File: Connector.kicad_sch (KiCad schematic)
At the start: 2 parts, among them J1 Conn_01x19, J2 Conn_01x19

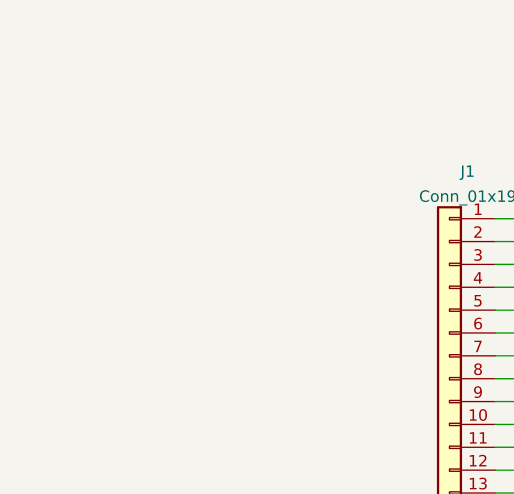
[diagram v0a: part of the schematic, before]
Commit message: Routed most PCB traces
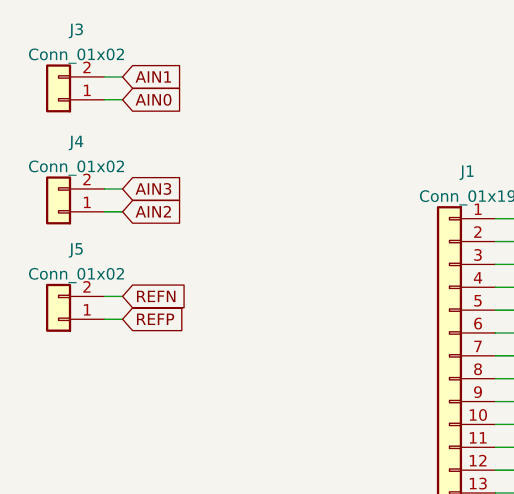
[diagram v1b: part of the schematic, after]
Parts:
- added J3, J4, J5: Conn_01x02, Connector_Molex:Molex_CLIK-Mate_502382-0270_1x02-1MP_P1.25mm_Vertical, symbol Connector_Generic:Conn_01x02
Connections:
- new net AIN0: J3.1 (Pin_1)
- new net AIN1: J3.2 (Pin_2)
- new net AIN2: J4.1 (Pin_1)
- new net AIN3: J4.2 (Pin_2)
- new net REFN: J5.2 (Pin_2)
- new net REFP: J5.1 (Pin_1)
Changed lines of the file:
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@@
   (junction (at 138.684 88.392) (diameter 1.016) (color 0 0 0 0))
   (junction (at 145.034 73.152) (diameter 1.016) (color 0 0 0 0))
+  (wire (pts (xy 48.514 57.404) (xy 50.546 57.404))
+    (stroke (width 0) (type solid) (color 0 0 0 0))
+  )
+  (wire (pts (xy 48.514 59.944) (xy 50.546 59.944))
+    (stroke (width 0) (type solid) (color 0 0 0 0))
+  )
+  (wire (pts (xy 48.514 69.85) (xy 50.546 69.85))
+    (stroke (width 0) (type solid) (color 0 0 0 0))
+  )
+  (wire (pts (xy 48.514 72.39) (xy 50.546 72.39))
+    (stroke (width 0) (type solid) (color 0 0 0 0))
+  )
+  (wire (pts (xy 48.514 81.788) (xy 50.546 81.788))
+    (stroke (width 0) (type solid) (color 0 0 0 0))
+  )
+  (wire (pts (xy 48.514 84.328) (xy 50.546 84.328))
+    (stroke (width 0) (type solid) (color 0 0 0 0))
+  )
   (wire (pts (xy 91.948 73.152) (xy 99.06 73.152))
     (stroke (width 0) (type solid) (color 0 0 0 0))
@@
   (wire (pts (xy 149.098 71.12) (xy 149.098 73.152))
     (stroke (width 0) (type solid) (color 0 0 0 0))
+  )
+  (global_label "AIN1" (shape input) (at 50.546 57.404 0) (fields_autoplaced)
+    (effects (font (size 1.27 1.27)) (justify left))
+    (property "Intersheet References" "${INTERSHEET_REFS}" (id 0) (at 57.0971 57.3246 0)
+      (effects (font (size 1.27 1.27)) (justify left) hide)
+    )
+  )
+  (global_label "AIN0" (shape input) (at 50.546 59.944 0) (fields_autoplaced)
+    (effects (font (size 1.27 1.27)) (justify left))
+    (property "Intersheet References" "${INTERSHEET_REFS}" (id 0) (at 57.0971 59.8646 0)
+      (effects (font (size 1.27 1.27)) (justify left) hide)
+    )
+  )
+  (global_label "AIN3" (shape input) (at 50.546 69.85 0) (fields_autoplaced)
+    (effects (font (size 1.27 1.27)) (justify left))
+    (property "Intersheet References" "${INTERSHEET_REFS}" (id 0) (at 57.0971 69.7706 0)
+      (effects (font (size 1.27 1.27)) (justify left) hide)
+    )
+  )
+  (global_label "AIN2" (shape input) (at 50.546 72.39 0) (fields_autoplaced)
+    (effects (font (size 1.27 1.27)) (justify left))
+    (property "Intersheet References" "${INTERSHEET_REFS}" (id 0) (at 57.0971 72.3106 0)
+      (effects (font (size 1.27 1.27)) (justify left) hide)
+    )
+  )
+  (global_label "REFN" (shape input) (at 50.546 81.788 0) (fields_autoplaced)
+    (effects (font (size 1.27 1.27)) (justify left))
+    (property "Intersheet References" "${INTERSHEET_REFS}" (id 0) (at 57.7019 81.7086 0)
+      (effects (font (size 1.27 1.27)) (justify left) hide)
+    )
+  )
+  (global_label "REFP" (shape input) (at 50.546 84.328 0) (fields_autoplaced)
+    (effects (font (size 1.27 1.27)) (justify left))
+    (property "Intersheet References" "${INTERSHEET_REFS}" (id 0) (at 57.6414 84.2486 0)
+      (effects (font (size 1.27 1.27)) (justify left) hide)
+    )
   )
   (global_label "SENSOR_VP" (shape input) (at 100.076 78.232 0) (fields_autoplaced)
@@
     (pin "1")
   )
+  (symbol (lib_id "Connector_Generic:Conn_01x02") (at 43.434 59.944 180) (unit 1)
+    (in_bom yes) (on_board yes) (fields_autoplaced)
+    (property "Reference" "J3" (id 0) (at 45.466 52.1674 0))
+    (property "Value" "Conn_01x02" (id 1) (at 45.466 54.9425 0))
+    (property "Footprint" "Connector_Molex:Molex_CLIK-Mate_502382-0270_1x02-1MP_P1.25mm_Vertical" (id 2) (at 43.434 59.944 0)
+      (effects (font (size 1.27 1.27)) hide)
+    )
+    (property "Datasheet" "~" (id 3) (at 43.434 59.944 0)
+      (effects (font (size 1.27 1.27)) hide)
+    )
+    (pin "1")
+    (pin "2")
+  )
+  (symbol (lib_id "Connector_Generic:Conn_01x02") (at 43.434 72.39 180) (unit 1)
+    (in_bom yes) (on_board yes) (fields_autoplaced)
+    (property "Reference" "J4" (id 0) (at 45.466 64.6134 0))
+    (property "Value" "Conn_01x02" (id 1) (at 45.466 67.3885 0))
+    (property "Footprint" "Connector_Molex:Molex_CLIK-Mate_502382-0270_1x02-1MP_P1.25mm_Vertical" (id 2) (at 43.434 72.39 0)
+      (effects (font (size 1.27 1.27)) hide)
+    )
+    (property "Datasheet" "~" (id 3) (at 43.434 72.39 0)
+      (effects (font (size 1.27 1.27)) hide)
+    )
+    (pin "1")
+    (pin "2")
+  )
+  (symbol (lib_id "Connector_Generic:Conn_01x02") (at 43.434 84.328 180) (unit 1)
+    (in_bom yes) (on_board yes) (fields_autoplaced)
+    (property "Reference" "J5" (id 0) (at 45.466 76.5514 0))
+    (property "Value" "Conn_01x02" (id 1) (at 45.466 79.3265 0))
+    (property "Footprint" "Connector_Molex:Molex_CLIK-Mate_502382-0270_1x02-1MP_P1.25mm_Vertical" (id 2) (at 43.434 84.328 0)
+      (effects (font (size 1.27 1.27)) hide)
+    )
+    (property "Datasheet" "~" (id 3) (at 43.434 84.328 0)
+      (effects (font (size 1.27 1.27)) hide)
+    )
+    (pin "1")
+    (pin "2")
+  )
   (symbol (lib_id "Connector_Generic:Conn_01x19") (at 86.868 96.012 0) (mirror y) (unit 1)

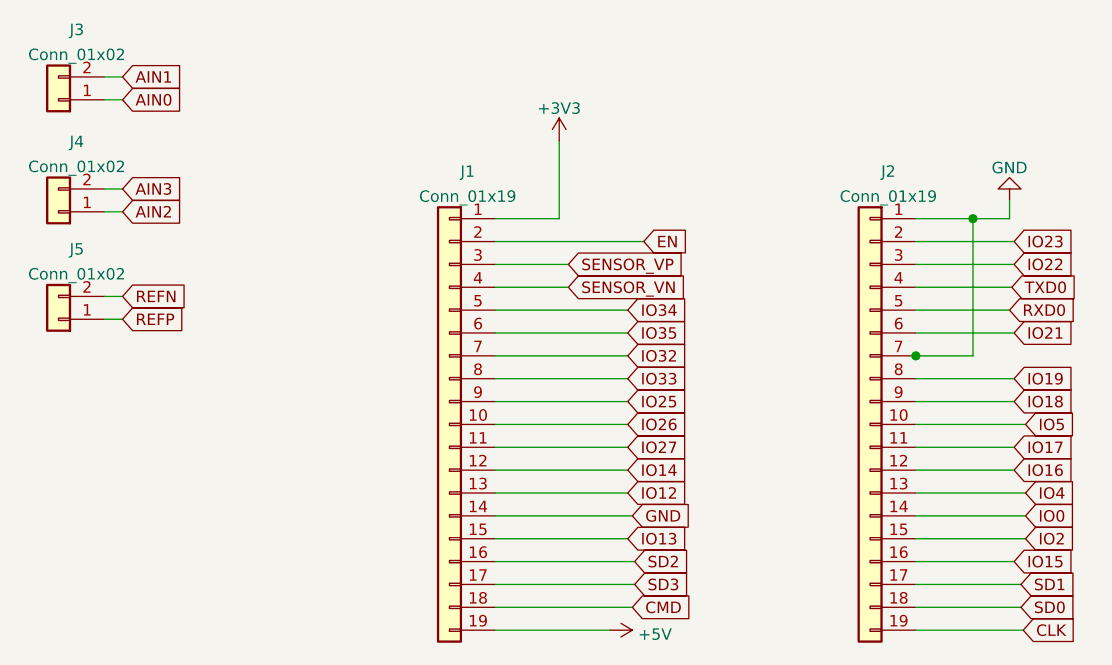
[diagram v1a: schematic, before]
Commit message: Added VOC and Optical Sensors
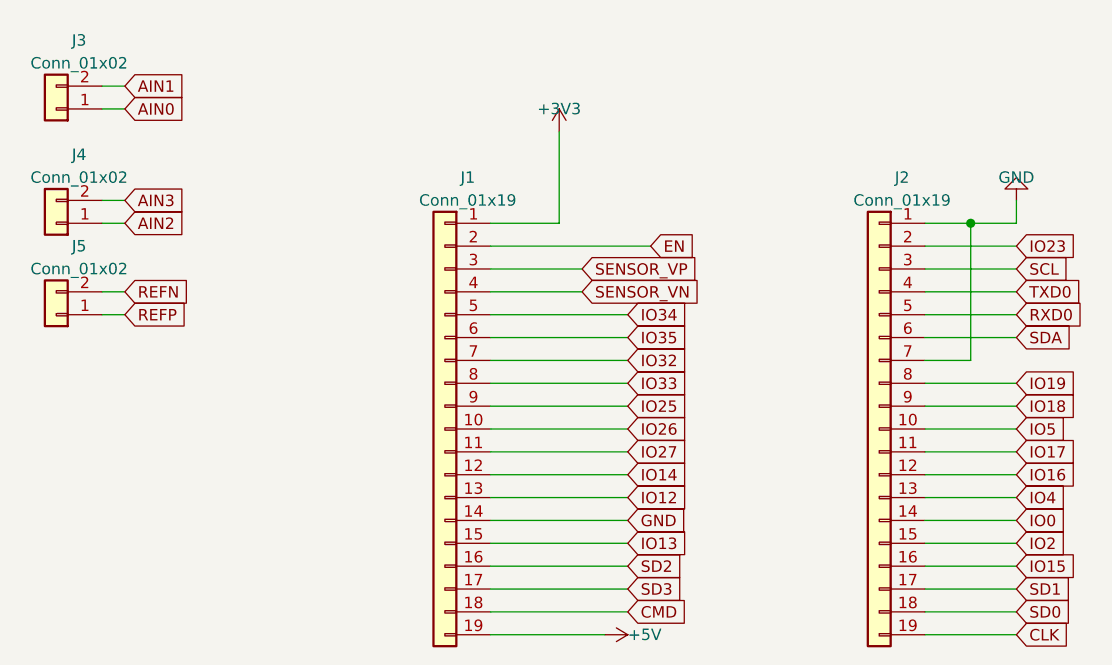
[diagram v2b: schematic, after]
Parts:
- J1, J2: footprint Connector_PinHeader_1.00mm:PinHeader_1x19_P1.00mm_Vertical -> Connector_PinHeader_2.54mm:PinHeader_1x19_P2.54mm_Vertical
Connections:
- net IO21 renamed SDA
- net IO22 renamed SCL
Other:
- moved on the sheet: J1, J2, J3, J4, J5

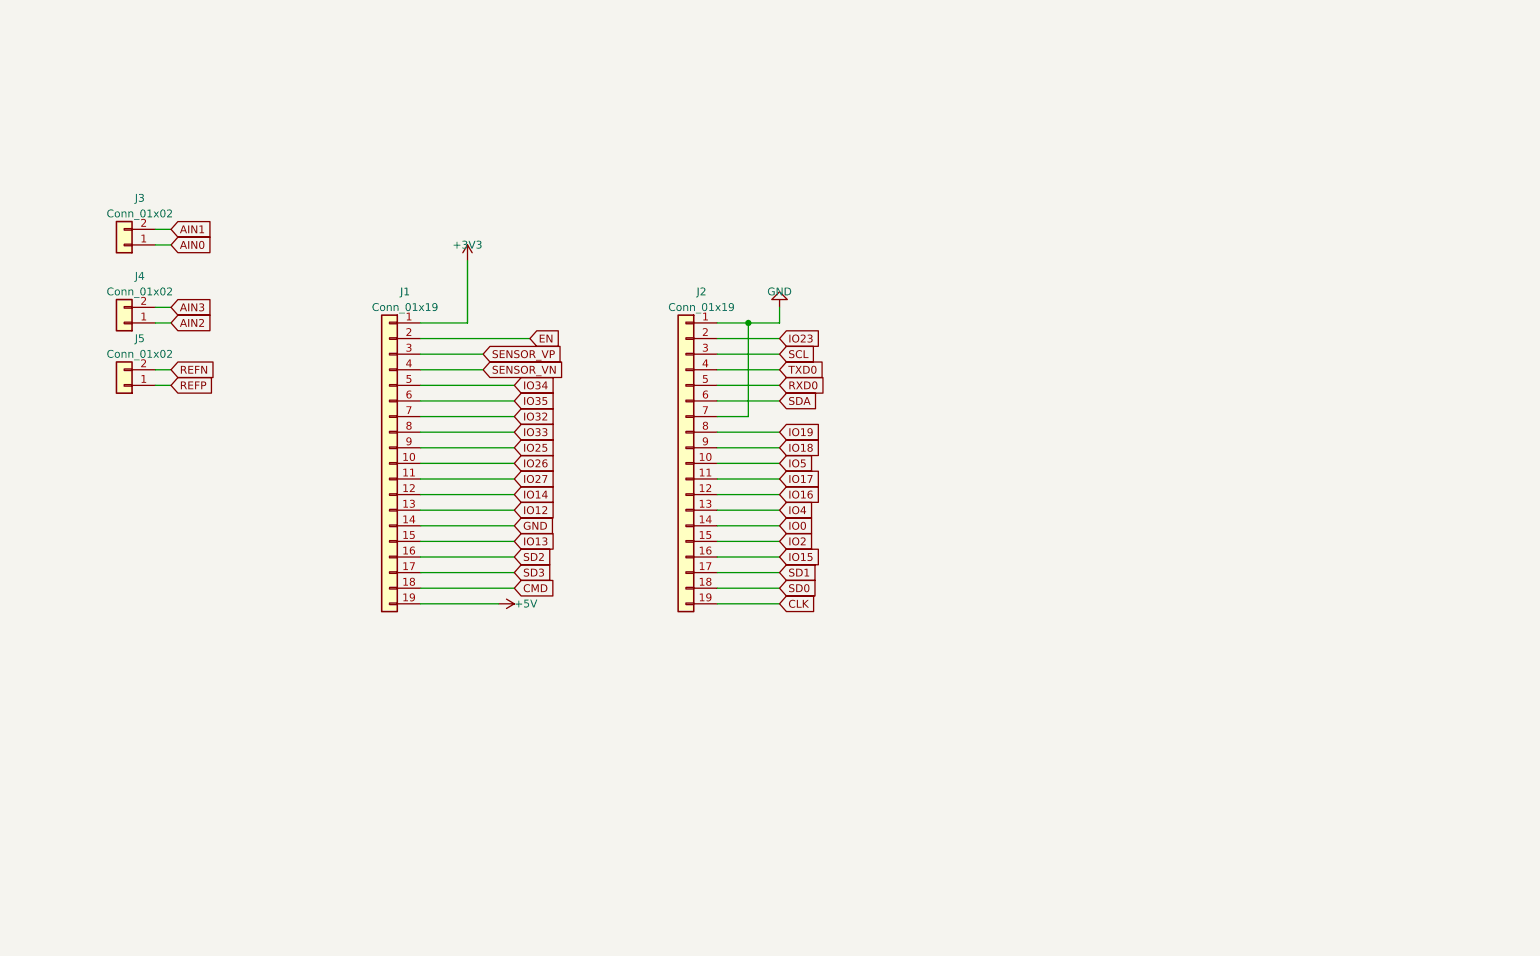
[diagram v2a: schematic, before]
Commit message: Vertical Horizontal Traces
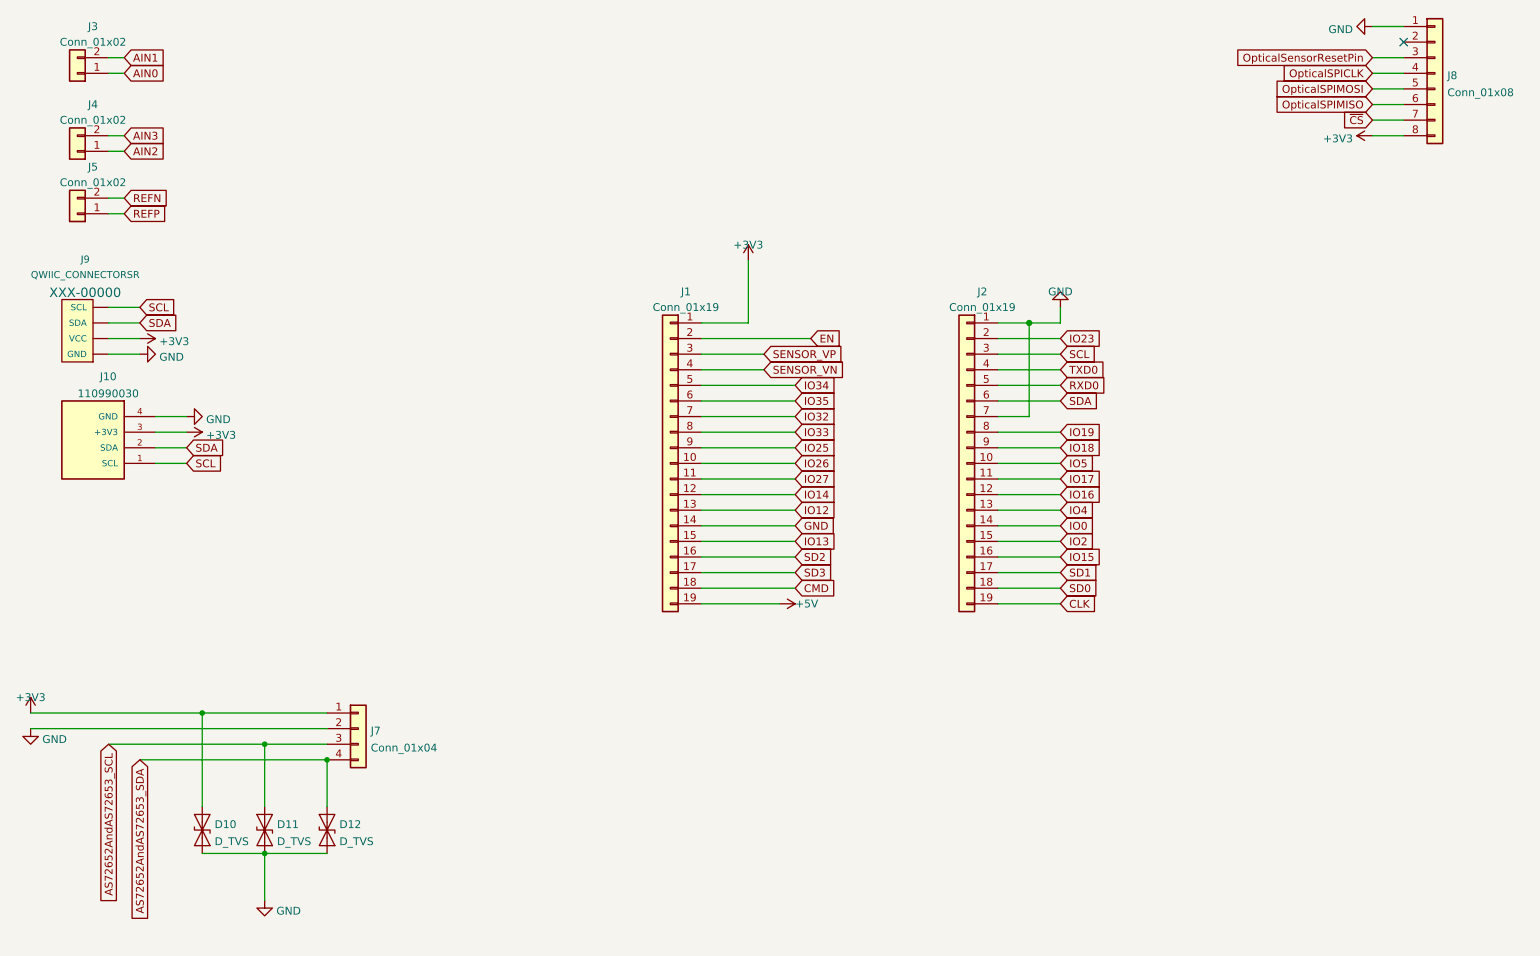
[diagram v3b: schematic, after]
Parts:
- added D10, D11, D12: D_TVS, Diode_SMD:D_0402_1005Metric_Pad0.77x0.64mm_HandSolder, symbol Device:D_TVS
- added J10: 110990030, Seeed:SEEED_110990030, symbol Seeed4Pin2mmFemale:110990030
- added J7: Conn_01x04, Connector_PinHeader_2.54mm:PinHeader_1x04_P2.54mm_Vertical, symbol Connector_Generic:Conn_01x04
- added J8: Conn_01x08, Connector_PinHeader_2.54mm:PinHeader_1x08_P2.54mm_Vertical, symbol Connector_Generic:Conn_01x08
- added J9: QWIIC_CONNECTORSR, SparkfunConnectors:1X04_1MM_RA_STRESSRELIEF, symbol SparkFun-Connectors:QWIIC_CONNECTORSR
- J3, J4, J5: footprint Connector_Molex:Molex_CLIK-Mate_502382-0270_1x02-1MP_P1.25mm_Vertical -> Connector_PinHeader_2.54mm:PinHeader_1x02_P2.54mm_Vertical
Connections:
- net +3V3: now also D10.2 (A2), J10.3 (+3V3), J7.1 (Pin_1), J8.8 (Pin_8), J9.2 (VCC)
- net GND: now also D10.1 (A1), D11.1 (A1), D12.1 (A1), J10.4 (GND), J7.2 (Pin_2), J8.1 (Pin_1), J9.1 (GND)
- net SCL: now also J10.1 (SCL), J9.4 (SCL)
- net SDA: now also J10.2 (SDA), J9.3 (SDA)
- new net AS72652AndAS72653_SCL: D11.2 (A2), J7.3 (Pin_3)
- new net AS72652AndAS72653_SDA: D12.2 (A2), J7.4 (Pin_4)
- new net OpticalSPICLK: J8.4 (Pin_4)
- new net OpticalSPIMISO: J8.6 (Pin_6)
- new net OpticalSPIMOSI: J8.5 (Pin_5)
- new net OpticalSensorResetPin: J8.3 (Pin_3)
- new net ~{CS}: J8.7 (Pin_7)
- no-connect marks 0 -> 1
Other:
- moved on the sheet: J1, J2, J3, J4, J5
